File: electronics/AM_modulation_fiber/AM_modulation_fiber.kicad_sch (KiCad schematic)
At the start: 4 parts

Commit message: Update AM_modulation_filter
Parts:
- added C1, C2: 10u, symbol Device:C_Polarized
- added C3: 1u, symbol Device:C
- added J1: Alim_VCC, symbol Connector_Generic:Conn_01x03
- added R3, R4, R5, R6: 47k, Resistor_THT:R_Axial_DIN0207_L6.3mm_D2.5mm_P10.16mm_Horizontal, symbol Device:R
- added R7: 1k, Resistor_THT:R_Axial_DIN0207_L6.3mm_D2.5mm_P10.16mm_Horizontal, symbol Device:R
- added R8: 100k, Resistor_THT:R_Axial_DIN0207_L6.3mm_D2.5mm_P10.16mm_Horizontal, symbol Device:R
- added R9: 680k, Resistor_THT:R_Axial_DIN0207_L6.3mm_D2.5mm_P10.16mm_Horizontal, symbol Device:R
- added RV1: 1k, symbol Device:R_Potentiometer_Trim
- added U1: TL082, symbol Amplifier_Operational:TL082
- added U2: AD633ANZ, AD633ANZ:DIP254P762X533-8, symbol AD633ANZ:AD633ANZ
- R1: value R -> 180
- R2: value R -> 47k
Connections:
- net GND: now also R1.2, C1.2, C2.1, J1.2 (Pin_2), R4.1, R7.1, R8.2, R9.2, RV1.3
- net OUT_LED: now reaches XR1.A
- net OUT_LED: now also R3.2, U1.1
- net I_LED: now reaches XR1.K
- net I_LED: now also R1.1
- net VS_PHD: now reaches XR2.A
- net VS_PHD: now also C3.1, R8.1
- net VCC+: now reaches XR2.K
- net VCC+: now also C1.1, J1.3 (Pin_3), RV1.1, U1.8 (V+)
- net Offset: now reaches R2.1
- net Offset: now also RV1.2
- net at R2.2: now also R5.2, R6.2, U1.3 (+)
- new net: R3.1, R4.2, U1.2 (-)
- new net: C3.2, R9.1, U1.5 (+)
- new net IN_1: R6.1
- new net IN_2: R5.1, R7.2
- new net OUT_PHD: U1.6 (-), U1.7
- new net VCC-: C2.2, J1.1 (Pin_1), U1.4 (V-)
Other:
- moved on the sheet: R1, XR1, XR2

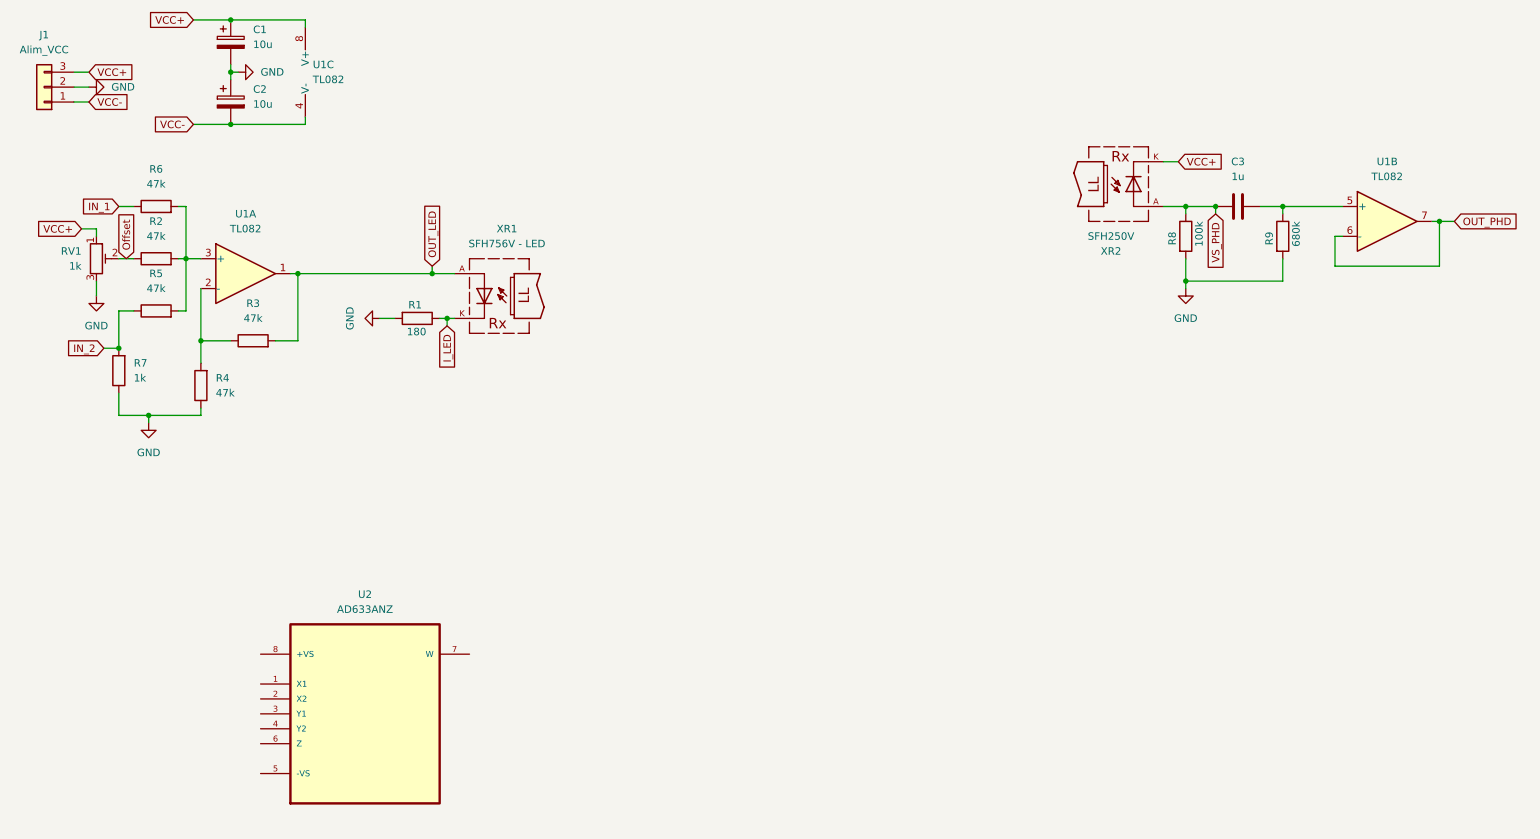
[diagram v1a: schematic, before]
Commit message: Update AM Modulation and Fiber transmission / demo and labwork
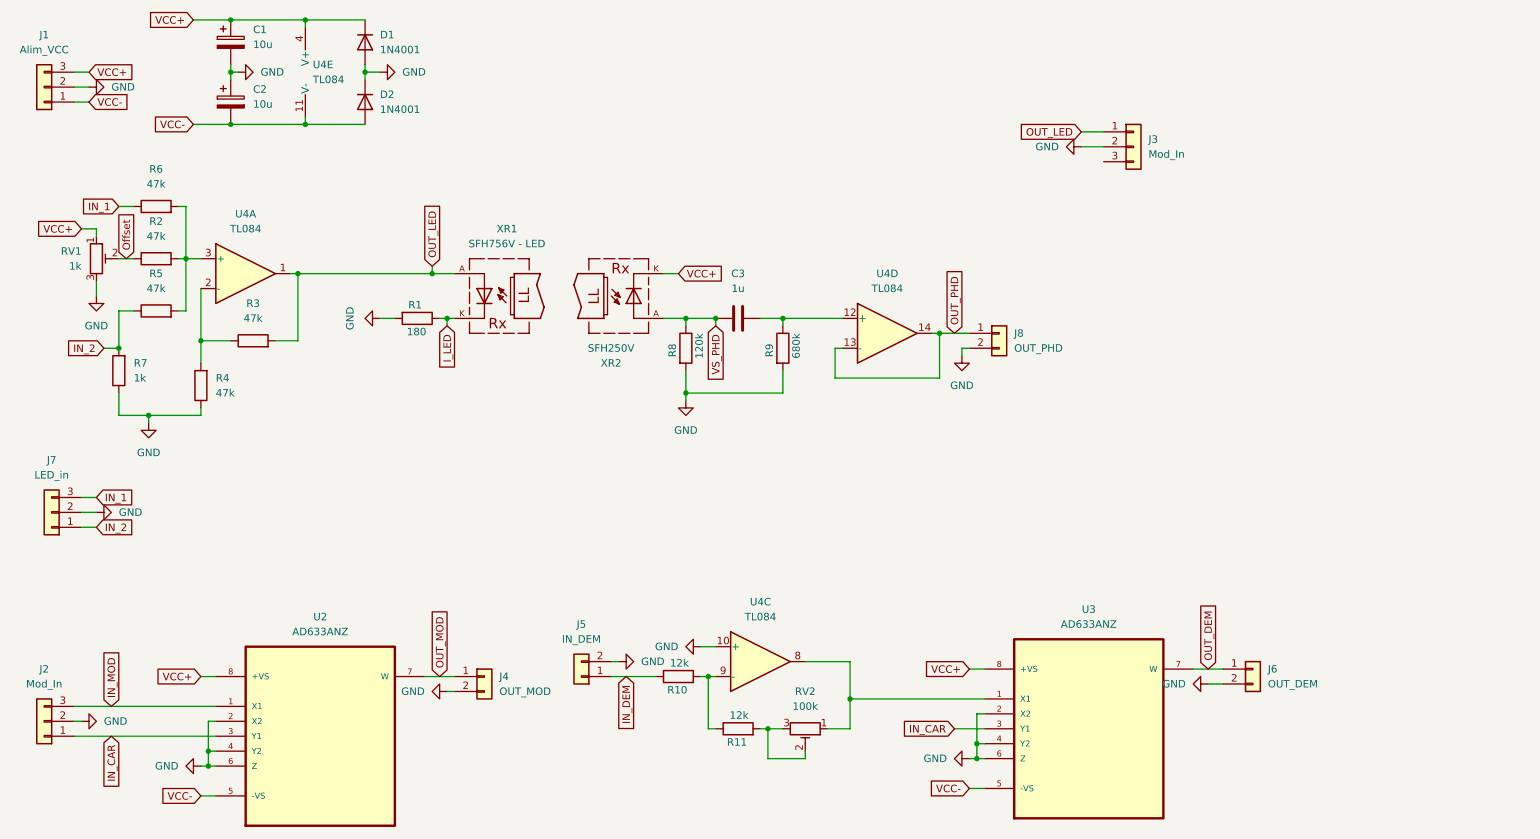
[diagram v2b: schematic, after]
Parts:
- removed U1: TL082, symbol Amplifier_Operational:TL082
- added D1, D2: 1N4001, Diode_THT:D_DO-41_SOD81_P10.16mm_Horizontal, symbol Diode:1N4001
- added J2, J3: Mod_In, Connector_PinHeader_2.54mm:PinHeader_1x03_P2.54mm_Vertical, symbol Connector_Generic:Conn_01x03
- added J4: OUT_MOD, Connector_PinHeader_2.54mm:PinHeader_1x02_P2.54mm_Vertical, symbol Connector_Generic:Conn_01x02
- added J5: IN_DEM, Connector_PinHeader_2.54mm:PinHeader_1x02_P2.54mm_Vertical, symbol Connector_Generic:Conn_01x02
- added J6: OUT_DEM, Connector_PinHeader_2.54mm:PinHeader_1x02_P2.54mm_Vertical, symbol Connector_Generic:Conn_01x02
- added J7: LED_in, Connector_PinHeader_2.54mm:PinHeader_1x03_P2.54mm_Vertical, symbol Connector_Generic:Conn_01x03
- added J8: OUT_PHD, Connector_PinHeader_2.54mm:PinHeader_1x02_P2.54mm_Vertical, symbol Connector_Generic:Conn_01x02
- added R10, R11: 12k, Resistor_THT:R_Axial_DIN0207_L6.3mm_D2.5mm_P10.16mm_Horizontal, symbol Device:R
- added RV2: 100k, Potentiometer_THT:Potentiometer_Bourns_3386P_Vertical, symbol Device:R_Potentiometer_Trim
- added U3: AD633ANZ, Package_DIP:DIP-8_W7.62mm_Socket_LongPads, symbol AD633ANZ:AD633ANZ
- added U4: TL084, Package_DIP:DIP-14_W7.62mm_Socket_LongPads, symbol Amplifier_Operational:TL084
- C1, C2: footprint (none) -> Capacitor_THT:CP_Radial_D8.0mm_P5.00mm
- C3: footprint (none) -> Capacitor_THT:C_Rect_L4.6mm_W3.8mm_P2.50mm_MKS02_FKP02
- J1: footprint (none) -> Connector_PinHeader_2.54mm:PinHeader_1x03_P2.54mm_Vertical
- R8: value 100k -> 120k
- RV1: footprint (none) -> Potentiometer_THT:Potentiometer_Bourns_3386P_Vertical
- U2: footprint AD633ANZ:DIP254P762X533-8 -> Package_DIP:DIP-8_W7.62mm_Socket_LongPads
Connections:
- net GND: now also U2.2 (X2), U2.4 (Y2), U2.6 (Z), D1.2 (A), D2.1 (K), J2.2 (Pin_2), J3.2 (Pin_2), J4.2 (Pin_2), J5.2 (Pin_2), J6.2 (Pin_2), J7.2 (Pin_2), J8.2 (Pin_2), U3.2 (X2), U3.4 (Y2), U3.6 (Z), U4.10 (+)
- net IN_1: now also J7.3 (Pin_3)
- net IN_2: now also J7.1 (Pin_1)
- net OUT_LED: now also J3.1 (Pin_1), U4.1
- net OUT_PHD: now also J8.1 (Pin_1), U4.13 (-), U4.14
- net VCC+: now also U2.8 (+VS), D1.1 (K), U3.8 (+VS), U4.4 (V+)
- net VCC-: now also U2.5 (-VS), D2.2 (A), U3.5 (-VS), U4.11 (V-)
- net at R2.2, R5.2, R6.2: now also U4.3 (+)
- net at R3.1, R4.2: now also U4.2 (-)
- net IN_MOD: now reaches U2.1 (X1)
- net IN_MOD: now also J2.3 (Pin_3)
- net IN_CAR: now reaches U2.3 (Y1)
- net IN_CAR: now also J2.1 (Pin_1), U3.3 (Y1)
- net OUT_MOD: now reaches U2.7 (W)
- net OUT_MOD: now also J4.1 (Pin_1)
- net at C3.2, R9.1: now also U4.12 (+)
- new net: RV2.1, U3.1 (X1), U4.8
- new net: R11.2, RV2.2, RV2.3
- new net: R10.2, R11.1, U4.9 (-)
- new net IN_DEM: J5.1 (Pin_1), R10.1
- new net OUT_DEM: J6.1 (Pin_1), U3.7 (W)
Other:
- moved on the sheet: C3, R8, R9, U2, XR2

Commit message: Update AM_Modulation_Fiber circuit
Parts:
- added J9: Mod_In, Connector_PinHeader_2.54mm:PinHeader_1x03_P2.54mm_Vertical, symbol Connector_Generic:Conn_01x03
- C1, C2: footprint Capacitor_THT:CP_Radial_D8.0mm_P5.00mm -> Capacitor_THT:CP_Radial_D6.3mm_P2.50mm
- C3: footprint Capacitor_THT:C_Rect_L4.6mm_W3.8mm_P2.50mm_MKS02_FKP02 -> Capacitor_THT:C_Rect_L7.0mm_W4.5mm_P5.00mm
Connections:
- net GND: now also J9.1 (Pin_1)
- net OUT_LED: now also J9.3 (Pin_3)
- net VCC+: now also J9.2 (Pin_2)
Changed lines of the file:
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@@
 	(wire
 		(pts
+			(xy 93.98 39.37) (xy 96.52 39.37)
+		)
+		(stroke
+			(width 0)
+			(type default)
+		)
+	)
+	(wire
+		(pts
 			(xy 156.21 69.85) (xy 154.94 69.85)
 		)
@@
 	(wire
 		(pts
+			(xy 93.98 36.83) (xy 96.52 36.83)
+		)
+		(stroke
+			(width 0)
+			(type default)
+		)
+	)
+	(wire
+		(pts
 			(xy 25.4 135.89) (xy 49.53 135.89)
 		)
@@
 	(wire
 		(pts
+			(xy 93.98 34.29) (xy 96.52 34.29)
+		)
+		(stroke
+			(width 0)
+			(type default)
+		)
+	)
+	(wire
+		(pts
 			(xy 88.9 64.77) (xy 90.17 64.77)
 		)
@@
 		)
 	)
+	(global_label "OUT_LED"
+		(shape input)
+		(at 93.98 39.37 180)
+		(fields_autoplaced yes)
+		(effects
+			(font
+				(size 1.27 1.27)
+			)
+			(justify right)
+		)
+		(property "Intersheetrefs" "${INTERSHEET_REFS}"
+			(at 82.9515 39.37 0)
+			(effects
+				(font
+					(size 1.27 1.27)
+				)
+				(justify right)
+				(hide yes)
+			)
+		)
+	)
 	(global_label "IN_2"
 		(shape input)
@@
 		)
 	)
+	(global_label "VCC+"
+		(shape input)
+		(at 93.98 36.83 180)
+		(fields_autoplaced yes)
+		(effects
+			(font
+				(size 1.27 1.27)
+			)
+			(justify right)
+		)
+		(property "Intersheetrefs" "${INTERSHEET_REFS}"
+			(at 85.7938 36.83 0)
+			(effects
+				(font
+					(size 1.27 1.27)
+				)
+				(justify right)
+				(hide yes)
+			)
+		)
+	)
 	(symbol
 		(lib_id "power:GND")
@@
 	)
 	(symbol
+		(lib_id "Connector_Generic:Conn_01x03")
+		(at 101.6 36.83 0)
+		(unit 1)
+		(exclude_from_sim no)
+		(in_bom yes)
+		(on_board yes)
+		(dnp no)
+		(fields_autoplaced yes)
+		(property "Reference" "J9"
+			(at 104.14 35.5599 0)
+			(effects
+				(font
+					(size 1.27 1.27)
+				)
+				(justify left)
+			)
+		)
+		(property "Value" "Mod_In"
+			(at 104.14 38.0999 0)
+			(effects
+				(font
+					(size 1.27 1.27)
+				)
+				(justify left)
+			)
+		)
+		(property "Footprint" "Connector_PinHeader_2.54mm:PinHeader_1x03_P2.54mm_Vertical"
+			(at 101.6 36.83 0)
+			(effects
+				(font
+					(size 1.27 1.27)
+				)
+				(hide yes)
+			)
+		)
+		(property "Datasheet" "~"
+			(at 101.6 36.83 0)
+			(effects
+				(font
+					(size 1.27 1.27)
+				)
+				(hide yes)
+			)
+		)
+		(property "Description" "Generic connector, single row, 01x03, script generated (kicad-library-utils/schlib/autogen/connector/)"
+			(at 101.6 36.83 0)
+			(effects
+				(font
+					(size 1.27 1.27)
+				)
+				(hide yes)
+			)
+		)
+		(pin "1"
+		)
+		(pin "3"
+		)
+		(pin "2"
+		)
+		(instances
+			(project "AM_modulation_fiber"
+				(path "/321de10e-4c5a-4709-a860-0ca07d993626"
+					(reference "J9")
+					(unit 1)
+				)
+			)
+		)
+	)
+	(symbol
 		(lib_id "Device:R")
 		(at 39.37 63.5 90)
@@
 			)
 		)
-		(property "Footprint" "Capacitor_THT:CP_Radial_D8.0mm_P5.00mm"
+		(property "Footprint" "Capacitor_THT:CP_Radial_D6.3mm_P2.50mm"
 			(at 53.0352 31.75 0)
 			(effects
@@
 			)
 		)
-		(property "Footprint" "Capacitor_THT:C_Rect_L4.6mm_W3.8mm_P2.50mm_MKS02_FKP02"
+		(property "Footprint" "Capacitor_THT:C_Rect_L7.0mm_W4.5mm_P5.00mm"
 			(at 142.24 63.8048 0)
 			(effects
@@
 			)
 		)
-		(property "Footprint" "Capacitor_THT:CP_Radial_D8.0mm_P5.00mm"
+		(property "Footprint" "Capacitor_THT:CP_Radial_D6.3mm_P2.50mm"
 			(at 53.0352 21.59 0)
 			(effects
@@
 				)
 			)
+		)
+	)
+	(symbol
+		(lib_id "power:GND")
+		(at 93.98 34.29 270)
+		(unit 1)
+		(exclude_from_sim no)
+		(in_bom yes)
+		(on_board yes)
+		(dnp no)
+		(fields_autoplaced yes)
+		(property "Reference" "#PWR018"
+			(at 87.63 34.29 0)
+			(effects
+				(font
+					(size 1.27 1.27)
+				)
+				(hide yes)
+			)
+		)
+		(property "Value" "GND"
+			(at 88.9 34.29 0)
+			(effects
+				(font
+					(size 1.27 1.27)
+				)
+			)
+		)
+		(property "Footprint" ""
+			(at 93.98 34.29 0)
+			(effects
+				(font
+					(size 1.27 1.27)
+				)
+				(hide yes)
+			)
+		)
+		(property "Datasheet" ""
+			(at 93.98 34.29 0)
+			(effects
+				(font
+					(size 1.27 1.27)
+				)
+				(hide yes)
+			)
+		)
+		(property "Description" "Power symbol creates a global label with name \"GND\" , ground"
+			(at 93.98 34.29 0)
+			(effects
+				(font
+					(size 1.27 1.27)
+				)
+				(hide yes)
+			)
+		)
+		(pin "1"
+		)
+		(instances
+			(project "AM_modulation_fiber"
+				(path "/321de10e-4c5a-4709-a860-0ca07d993626"
+					(reference "#PWR018")
+					(unit 1)
+				)
+			)

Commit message: Update AM_Modulation_Fiber
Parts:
- J3: value Mod_In -> PhD_OUT
- J8: value OUT_PHD -> OUT_LED
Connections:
- net OUT_LED: now also J8.1 (Pin_1); no longer J3.1 (Pin_1)
- net OUT_PHD: now also J3.1 (Pin_1); no longer J8.1 (Pin_1)
- net VS_PHD: now also J3.3 (Pin_3)
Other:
- moved on the sheet: J3, J8
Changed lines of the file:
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@@
 	(wire
 		(pts
-			(xy 176.53 69.85) (xy 176.53 71.12)
-		)
-		(stroke
-			(width 0)
-			(type default)
-		)
-	)
-	(wire
-		(pts
 			(xy 29.21 58.42) (xy 29.21 60.96)
 		)
@@
 	(wire
 		(pts
+			(xy 177.8 72.39) (xy 177.8 73.66)
+		)
+		(stroke
+			(width 0)
+			(type default)
+		)
+	)
+	(wire
+		(pts
 			(xy 86.36 55.88) (xy 86.36 57.15)
 		)
@@
 	(wire
 		(pts
+			(xy 175.26 71.12) (xy 175.26 69.85)
+		)
+		(stroke
+			(width 0)
+			(type default)
+		)
+	)
+	(wire
+		(pts
 			(xy 88.9 64.77) (xy 90.17 64.77)
 		)
@@
 	(wire
 		(pts
-			(xy 26.67 97.79) (xy 29.21 97.79)
+			(xy 175.26 69.85) (xy 177.8 69.85)
 		)
 		(stroke
@@
 	(wire
 		(pts
-			(xy 179.07 139.7) (xy 180.34 139.7)
+			(xy 26.67 97.79) (xy 29.21 97.79)
 		)
 		(stroke
@@
 	(wire
 		(pts
-			(xy 177.8 69.85) (xy 176.53 69.85)
+			(xy 179.07 139.7) (xy 180.34 139.7)
 		)
 		(stroke
@@
 		)
 	)
+	(global_label "VS_PHD"
+		(shape input)
+		(at 177.8 73.66 270)
+		(fields_autoplaced yes)
+		(effects
+			(font
+				(size 1.27 1.27)
+			)
+			(justify right)
+		)
+		(property "Intersheetrefs" "${INTERSHEET_REFS}"
+			(at 177.8 83.7814 90)
+			(effects
+				(font
+					(size 1.27 1.27)
+				)
+				(justify right)
+				(hide yes)
+			)
+		)
+	)
 	(global_label "IN_CAR"
 		(shape input)
@@
 	(symbol
 		(lib_id "Connector_Generic:Conn_01x03")
-		(at 205.74 35.56 0)
+		(at 182.88 69.85 0)
 		(unit 1)
 		(exclude_from_sim no)
@@
 		(fields_autoplaced yes)
 		(property "Reference" "J3"
-			(at 208.28 34.2899 0)
+			(at 185.42 68.5799 0)
 			(effects
 				(font
@@
 			)
 		)
-		(property "Value" "Mod_In"
-			(at 208.28 36.8299 0)
+		(property "Value" "PhD_OUT"
+			(at 185.42 71.1199 0)
 			(effects
 				(font
@@
 		)
 		(property "Footprint" "Connector_PinHeader_2.54mm:PinHeader_1x03_P2.54mm_Vertical"
-			(at 205.74 35.56 0)
+			(at 182.88 69.85 0)
 			(effects
 				(font
@@
 		)
 		(property "Datasheet" "~"
-			(at 205.74 35.56 0)
+			(at 182.88 69.85 0)
 			(effects
 				(font
@@
 		)
 		(property "Description" "Generic connector, single row, 01x03, script generated (kicad-library-utils/schlib/autogen/connector/)"
-			(at 205.74 35.56 0)
+			(at 182.88 69.85 0)
 			(effects
 				(font
@@
 	(symbol
 		(lib_id "power:GND")
-		(at 176.53 71.12 0)
+		(at 175.26 71.12 0)
 		(unit 1)
 		(exclude_from_sim no)
@@
 		(fields_autoplaced yes)
 		(property "Reference" "#PWR017"
-			(at 176.53 77.47 0)
+			(at 175.26 77.47 0)
 			(effects
 				(font
@@
 		)
 		(property "Value" "GND"
-			(at 176.53 76.2 0)
+			(at 175.26 76.2 0)
 			(effects
 				(font
@@
 		)
 		(property "Footprint" ""
-			(at 176.53 71.12 0)
+			(at 175.26 71.12 0)
 			(effects
 				(font
@@
 		)
 		(property "Datasheet" ""
-			(at 176.53 71.12 0)
+			(at 175.26 71.12 0)
 			(effects
 				(font
@@
 		)
 		(property "Description" "Power symbol creates a global label with name \"GND\" , ground"
-			(at 176.53 71.12 0)
+			(at 175.26 71.12 0)
 			(effects
 				(font
@@
 	(symbol
 		(lib_id "Connector_Generic:Conn_01x02")
-		(at 182.88 67.31 0)
+		(at 205.74 33.02 0)
 		(unit 1)
 		(exclude_from_sim no)
@@
 		(fields_autoplaced yes)
 		(property "Reference" "J8"
-			(at 185.42 67.3099 0)
+			(at 208.28 33.0199 0)
 			(effects
 				(font
@@
 			)
 		)
-		(property "Value" "OUT_PHD"
-			(at 185.42 69.8499 0)
+		(property "Value" "OUT_LED"
+			(at 208.28 35.5599 0)
 			(effects
 				(font
@@
 		)
 		(property "Footprint" "Connector_PinHeader_2.54mm:PinHeader_1x02_P2.54mm_Vertical"
-			(at 182.88 67.31 0)
+			(at 205.74 33.02 0)
 			(effects
 				(font
@@
 		)
 		(property "Datasheet" "~"
-			(at 182.88 67.31 0)
+			(at 205.74 33.02 0)
 			(effects
 				(font
@@
 		)
 		(property "Description" "Generic connector, single row, 01x02, script generated (kicad-library-utils/schlib/autogen/connector/)"
-			(at 182.88 67.31 0)
+			(at 205.74 33.02 0)
 			(effects
 				(font
